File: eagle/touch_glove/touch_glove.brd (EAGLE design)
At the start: 88.9 x 50.8 mm, 210 parts, among them J2 (ID,OD)=(2.1,5.5)MM, P1 PELTIER, P2 PELTIER, P3 PELTIER, P4 PELTIER, P5 PELTIER, SW1 5A/28V, SW2 5A/28V, U1 DRV8837C, U2 DRV8837C, U3 DRV8837C, U4 DRV8837C, U5 DRV8837C, Y2 16MHz

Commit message: Started on Touch Glove.  Going full ambitious using 0402 for resistors, capacitors, and inductors
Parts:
- removed BATT1: BATTERYPTH_HOLES, MrSwirlyEyes:DUAL_PTH_PADS
- removed C121, C129: 0.1uF/50V, PiB_capacitors:_CER_SMD-805
- removed C125, C128: 10uF/25V, PiB_capacitors:_CER_SMD-805
- removed C133: 100UF/16V, PiB_capacitors:_AE_SMD_L6.6-W6.6
- removed C2, C64, C66, C68, C70, C73, C75, C80: 0.1uF/50V, MrSwirlyEyes:CAP_CER_SMD-805
- removed C23, C63, C65, C69, C71, C72, C74, C77: 10uF/25V, MrSwirlyEyes:CAP_CER_SMD-805
- removed C67, C82: 220uF/16V, MrSwirlyEyes:CAP_POL_SMD_L6.6-W6.6
- removed C78, C81: 100UF/16V, MrSwirlyEyes:CAP_POL_SMD_L6.6-W6.6
- removed C79: 1uF/25V, MrSwirlyEyes:CAP_CER_SMD-805
- removed D10: 1A/50V, PiB_discrete_semiconductors:SOD123F
- removed D6, D7, D9: 1A/50V, MrSwirlyEyes:DIODE_SMD_1A-50V-SOD123F
- removed J2: (ID,OD)=(2.1,5.5)MM, PiB_connectors:POWER_JACK_SLOT_ID2.1MM-OD5.5MM
- removed L1, L2: 10uH, MrSwirlyEyes:INDUCTOR_SMD-805
- removed P1, P2, P3, P4, P5: PELTIER, MrSwirlyEyes:CONNECTOR_PELTIER
- removed PWM_DRIVER: PCA9685, MrSwirlyEyes:TSSOP-28
- removed SW1: 5A/28V, MrSwirlyEyes:SW-SLIDE_SPDT_5A-28V_13L-7W
- removed U$1, U$2: NET_BRIDGE, MrSwirlyEyes:NET_BRIDGE
- removed U1, U2, U3, U4, U5: DRV8837C, MrSwirlyEyes:WSON-8-PPAD
- removed VIBE_1, VIBE_2, VIBE_3, VIBE_4, VIBE_5, VIBE_6: VIBE_MOTOR, MrSwirlyEyes:CONNECTOR_VIBE-MOTOR
- removed VIBE_T1, VIBE_T2, VIBE_T3, VIBE_T4, VIBE_T5, VIBE_T6: 2.6A/20V/57mΩ, MrSwirlyEyes:SOT23-3
- removed VREG2: 1.5A/3.3V, MrSwirlyEyes:SOT223-4
- removed VREG3: 1A/3.3V, MrSwirlyEyes:SOIC-8_W3.9MM
- removed VREG4: 3A/1.8V, MrSwirlyEyes:DDPAK-5
- removed VREG5: 5A/5V, PiB_ic_power:TO-263-5
- added C36, C38, C40, C45, C47, C48, C49, C50, C51: 0.1uF/50V, PiB_capacitors:_CER_SMD_0402
- added C37, C44: 10uF/16V, PiB_capacitors:_CER_SMD-603
- added C39, C43: 10uF/10V, PiB_capacitors:_CER_SMD_0402
- added C41, C42, C46: 100uF, PiB_capacitors:_CER_SMD-1210
- added D13, D14: 1A/50V, MrSwirlyEyes:DIODE_SMD_1A-50V-SOD123F
- added FLEX10, FLEX6, FLEX7, FLEX8, FLEX9: 10K, PiB:CONNECTOR_FSR
- added HBRIDGE1, HBRIDGE2, HBRIDGE3, HBRIDGE4, HBRIDGE5: DRV8837C, PiB:WSON-8-PPAD
- added Q1, Q2, Q3, Q4, Q5, Q6: MCH3474 4A/30V/50mΩ, PiB_discrete_semiconductors:SC-70FL/MCPH3
- added R38, R39, R42, R43, R44: 10KΩ, PiB_resistors:RESISTOR_SMD-0402
- added TEC1, TEC2, TEC3, TEC4, TEC5: PELTIER, PiB:CONNECTOR_PELTIER
- added VIBE1, VIBE2, VIBE3, VIBE4, VIBE5, VIBE6: VIBE_MOTOR, PiB:CONNECTOR_VIBE-MOTOR
- added VREG6: TL1963A-33 1.5A/3.3V, PiB_ic_power:SOT223-4
- added VREG7: 3A/1.8V, MrSwirlyEyes:DDPAK-5
- C1, C12, C13, C16, C17, C20, C21, C24, C25, C26, C3, C30, C31, C32, C33, C34, C4, C5, C52, C53, C54, C55, C56, C6, C7, C8, C9: device MrSwirlyEyes:CAP_CER_SMD-805 -> PiB_capacitors:_CER_SMD_0402
- C10, C11, C14, C15, C18, C19, C22, C27, C28, C29, C35, C57, C58, C59, C60, C61: value 10uF/25V -> 10uF/10V; device MrSwirlyEyes:CAP_CER_SMD-805 -> PiB_capacitors:_CER_SMD_0402
- C100, C106, C108, C116, C117, C119, C122, C124, C127, C135, C98: device PiB_capacitors:_CER_SMD-805 -> PiB_capacitors:_CER_SMD_0402
- C107, C109, C110, C111, C132, C134, C136: device PiB_capacitors:_CER_SMD-805 -> PiB_capacitors:_CER_SMD-603
- C118: value 220uF/16V -> 100uF; device PiB_capacitors:_AE_SMD_L6.6-W6.6 -> PiB_capacitors:_CER_SMD-1210
- C120, C126: value 10uF/25V -> 10uF/16V; device PiB_capacitors:_CER_SMD-805 -> PiB_capacitors:_CER_SMD-603
- C123, C97, C99: value 10uF/25V -> 10uF/10V; device PiB_capacitors:_CER_SMD-805 -> PiB_capacitors:_CER_SMD_0402
- D1, D12, D2, D3, D4, D5: value 1A/50V -> 150mA/75V; device MrSwirlyEyes:DIODE_SMD_1A-50V-SOD123F -> PiB_discrete_semiconductors:SOD-923F/0402
- FLEX1, FLEX2, FLEX3, FLEX4, FLEX5: device MrSwirlyEyes:CONNECTOR_FSR -> PiB:CONNECTOR_FSR
- L5: device PiB_leds:LED_SMD-805_ -> PiB_leds:LED_SMD-0603_
- R1, R10, R11, R12, R13, R14, R15, R16, R17, R18, R19, R2, R20, R21, R22, R23, R24, R25, R26, R27, R28, R29, R3, R30, R31, R32, R33, R34, R35, R36, R37, R4, R5, R6, R7, R8, R9: device MrSwirlyEyes:RESISTOR_SMD-805 -> PiB_resistors:RESISTOR_SMD-0402
- R46, R47: device PiB_resistors:RESISTOR_SMD-805 -> PiB_resistors:RESISTOR_SMD-0402
- moved R12 433.0 mm to (28.6, 40.3), turned to 90 degrees
- moved D12 429.7 mm to (29.2, 45.1), turned to 180 degrees
- moved C24 429.3 mm to (61.0, -15.2)
- moved R13 428.8 mm to (27.6, 40.3), turned to 90 degrees
- moved C1 425.1 mm to (29.2, 46.1)
- moved C99 415.5 mm to (39.4, 31.0), turned to 90 degrees
- moved C35 414.7 mm to (-8.38, 45.0), turned to 270 degrees
- moved ANALOG_BR 410.5 mm to (137.2, -30.5)
- moved B2 410.5 mm to (177.8, -7.62)
- moved C106 410.5 mm to (101.6, -20.3)
- moved C107 410.5 mm to (101.6, -25.4)
- moved C108 410.5 mm to (109.2, -20.3)
- moved C109 410.5 mm to (106.7, -25.4)
- moved C110 410.5 mm to (111.8, -25.4)
- moved C111 410.5 mm to (116.8, -25.4)
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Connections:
- removed net 5V: C121.1, C125.1, C133.A, D10.A, VREG5.4
- removed net BATT_-: BATT2.-, J2.GND@2
- removed net C14: DEMUX1.17
- removed net C15: DEMUX1.16
- removed net FSR_1: FLEX1.-, R11.2
- removed net FSR_2: FLEX2.-, R34.2
- removed net FSR_3: FLEX3.-, R35.2
- removed net FSR_4: FLEX4.-, R36.2
- removed net FSR_5: FLEX5.-, R37.2
- removed net N$38: L2.2, U$2.P$1
- removed net N$40: C64.1, C66.1, C67.A, C68.1, C69.1, C71.1, C72.1, C73.1, C74.1, C78.A, D6.K, D7.K, D9.K, SW1.P$1, VREG2.1, VREG3.3, VREG3.4, VREG4.1, VREG4.2
- removed net N$43: BATT1.+, SW1.P$2
- removed net PWM10: PWM_DRIVER1.17
- removed net VM: C10.1, C13.1, C14.1, C17.1, C18.1, C21.1, C22.1, C26.1, C27.1, C9.1, U1.1, U2.1, U3.1, U4.1, U5.1
- new net 1.8V: C10.1, C13.1, C14.1, C17.1, C18.1, C21.1, C22.1, C26.1, C27.1, C39.1, C40.1, C42.1, C9.1, D14.A, HBRIDGE1.1, HBRIDGE2.1, HBRIDGE3.1, HBRIDGE4.1, HBRIDGE5.1, VREG7.4, VREG7.5
- new net C8: DEMUX1.23
- new net C9: DEMUX1.22
- net 3.3V: now also C1.1, C24.1, C3.1, C35.1, C36.1, C4.1, C41.1, C43.1, C5.1, C52.1, C53.1, C54.1, C55.1, C56.1, C57.1, C58.1, C59.1, C6.1, C60.1, C61.1, C7.1, D1.K, D12.K, D13.A, D2.K, D3.K, D4.K, D5.K, VIBE1.1, VIBE2.1, VIBE3.1, VIBE4.1, VIBE5.1, VIBE6.1, VREG6.3; no longer C65.1, C75.1, C77.1, C80.1, C81.A, C82.A, D7.A, D9.A, VREG2.3, VREG4.4, VREG4.5
- net AGND: now also C30.2, C31.2, C32.2, C33.2, C34.2, C47.2, C48.2, C49.2, C50.2, C51.2, R11.1, R34.1, R35.1, R36.1, R37.1, R38.1, R39.1, R42.1, R43.1, R44.1
- net AVCC: now also C30.1, C31.1, C32.1, C33.1, C34.1, C47.1, C48.1, C49.1, C50.1, C51.1, FLEX1.+, FLEX10.+, FLEX2.+, FLEX3.+, FLEX4.+, FLEX5.+, FLEX6.+, FLEX7.+, FLEX8.+, FLEX9.+
- net BATT_+: no longer J2.PWR
- net GND: now also BATT2.-, C118.2, C36.2, C37.2, C38.2, C39.2, C40.2, C41.2, C42.2, C43.2, C44.2, C45.2, C46.2, VREG6.2, VREG6.TAB, VREG7.3, VREG7.TAB; no longer BATT1.-, C10.2, C118.K, C13.2, C14.2, C17.2, C18.2, C2.2, C21.2, C22.2, C23.2, C24.2, C26.2, C27.2, C30.2, C31.2, C32.2, C33.2, C34.2, C35.2, C52.2, C53.2, C54.2, C55.2, C56.2, C57.2, C58.2, C59.2, C60.2, C61.2, C63.2, C64.2, C65.2, C66.2, C67.K, C68.2, C69.2, C70.2, C71.2, C72.2, C73.2, C74.2, C75.2, C77.2, C78.K, C80.2, C81.K, C82.K, C9.2, J2.GND@1, L2.1, PWM_DRIVER.1, PWM_DRIVER.14, PWM_DRIVER.2, PWM_DRIVER.23, PWM_DRIVER.24, PWM_DRIVER.25, PWM_DRIVER.3, PWM_DRIVER.4, PWM_DRIVER.5, R1.1, R11.1, R12.1, R2.1, R3.1, R34.1, R35.1, R36.1, R37.1, R4.1, R5.1, U$1.P$2, U1.4, U1.GND, U2.4, U2.GND, U3.4, U3.GND, U4.4, U4.GND, U5.4, U5.GND, VIBE_T1.S, VIBE_T2.S, VIBE_T3.S, VIBE_T4.S, VIBE_T5.S, VIBE_T6.S, VREG2.2, VREG2.4, VREG3.1, VREG3.2, VREG4.3, VREG4.TAB
- net N$1: now also HBRIDGE5.3, TEC5.HOT; no longer P1.HOT, U1.2
- net N$10: now also HBRIDGE4.6, R16.2; no longer U1.6
- net N$11: now also HBRIDGE4.3, TEC4.HOT; no longer P2.HOT, U2.2
- net N$12: now also HBRIDGE3.3, TEC3.HOT; no longer P2.COLD, U2.3
- net N$13: now also HBRIDGE3.5, R18.2; no longer U2.5
- net N$14: now also HBRIDGE3.6, R20.2; no longer U2.6
- net N$15: now also Q2.3, VIBE2.2; no longer VIBE_2.2, VIBE_T2.D
- net N$16: now also HBRIDGE3.2, TEC3.COLD; no longer P3.HOT, U3.2
- net N$17: now also Q1.3, VIBE1.2; no longer VIBE_1.2, VIBE_T1.D
- net N$18: now also HBRIDGE2.3, TEC2.HOT; no longer P3.COLD, U3.3
- net N$19: now also HBRIDGE2.5, R22.2; no longer U3.5
- net N$2: now also Q4.3, VIBE4.2; no longer VIBE_4.2, VIBE_T4.D
- net N$20: now also HBRIDGE2.6, R24.2; no longer U3.6
- net N$21: now also Q4.1, R4.2; no longer VIBE_T4.G
- net N$22: now also Q5.1, R5.2; no longer VIBE_T5.G
- net N$23: now also HBRIDGE2.2, TEC2.COLD; no longer P5.HOT, U5.2
- net N$24: now also HBRIDGE1.3, TEC1.HOT; no longer P5.COLD, U5.3
- net N$25: now also HBRIDGE1.5, R26.2; no longer U5.5
- net N$26: now also HBRIDGE1.6, R28.2; no longer U5.6
- net N$27: now also HBRIDGE1.2, TEC1.COLD; no longer P4.HOT, U4.2
- net N$28: now also Q1.1, R1.2, R6.2; no longer P4.COLD, U4.3
- net N$29: now also HBRIDGE5.5, R30.2; no longer U4.5
- net N$3: now also Q5.3, VIBE5.2; no longer VIBE_5.2, VIBE_T5.D
- net N$30: now also Q6.3, VIBE6.2; no longer VIBE_6.2, VIBE_T6.D
- net N$31: now also HBRIDGE5.6, R32.2; no longer U4.6
- net N$32: now also Q6.1, R12.2; no longer VIBE_T6.G
- net N$4: now also Q3.3, VIBE3.2; no longer VIBE_3.2, VIBE_T3.D
- net N$5: now also HBRIDGE5.2, TEC5.COLD; no longer P1.COLD, U1.3
- net N$53: now also L5.2; no longer L5.K
- net N$6: now also HBRIDGE4.2, TEC4.COLD; no longer R6.2, VIBE_T1.G
- net N$7: now also Q2.1, R2.2; no longer VIBE_T2.G
- net N$8: now also HBRIDGE4.5, R14.2; no longer U1.5
- net N$9: now also Q3.1, R3.2; no longer VIBE_T3.G
- net NGND: now also C10.2, C13.2, C14.2, C17.2, C18.2, C21.2, C22.2, C24.2, C26.2, C27.2, C35.2, C52.2, C53.2, C54.2, C55.2, C56.2, C57.2, C58.2, C59.2, C60.2, C61.2, C9.2, HBRIDGE1.4, HBRIDGE1.GND, HBRIDGE1.P$1, HBRIDGE1.P$2, HBRIDGE2.4, HBRIDGE2.GND, HBRIDGE2.P$1, HBRIDGE2.P$2, HBRIDGE3.4, HBRIDGE3.GND, HBRIDGE3.P$1, HBRIDGE3.P$2, HBRIDGE4.4, HBRIDGE4.GND, HBRIDGE4.P$1, HBRIDGE4.P$2, HBRIDGE5.4, HBRIDGE5.GND, HBRIDGE5.P$1, HBRIDGE5.P$2, Q1.2, Q2.2, Q3.2, Q4.2, Q5.2, Q6.2, R1.1, R12.1, R2.1, R3.1, R4.1, R5.1; no longer C121.2, C125.2, C128.2, C129.2, C133.K, C79.2, U$1.P$1, U$2.P$2, VREG5.3, VREG5.TAB
- net SCL: no longer PWM_DRIVER.26
- net SDA: no longer PWM_DRIVER.27
- net STRAIN_1: now also FLEX3.-, R35.2
- net STRAIN_10: now also DEMUX1.16, FLEX4.-, R36.2; no longer DEMUX1.22
- net STRAIN_2: now also FLEX2.-, R34.2
- net STRAIN_3: now also FLEX1.-, R11.2
- net STRAIN_4: now also FLEX10.-, R44.2
- net STRAIN_5: now also FLEX9.-, R43.2
- net STRAIN_6: now also FLEX8.-, R42.2
- net STRAIN_7: now also FLEX7.-, R39.2
- net STRAIN_8: now also FLEX6.-, R38.2
- net STRAIN_9: now also DEMUX1.17, FLEX5.-, R37.2; no longer DEMUX1.23
- net TEC_1_COLD: now also PWM_DRIVER1.18; no longer PWM_DRIVER.7, PWM_DRIVER1.7, R26.2
- net TEC_1_HOT: now also PWM_DRIVER1.17; no longer PWM_DRIVER.6, PWM_DRIVER1.6, R28.2
- net TEC_2_COLD: now also PWM_DRIVER1.20; no longer PWM_DRIVER.9, PWM_DRIVER1.9, R22.2
- net TEC_2_HOT: now also PWM_DRIVER1.19; no longer PWM_DRIVER.8, PWM_DRIVER1.8, R24.2
- net TEC_3_COLD: now also PWM_DRIVER1.22; no longer PWM_DRIVER.11, PWM_DRIVER1.11, R18.2
- net TEC_3_HOT: now also PWM_DRIVER1.21; no longer PWM_DRIVER.10, PWM_DRIVER1.10, R20.2
- net TEC_4_COLD: no longer PWM_DRIVER.13, R14.2
- net TEC_4_HOT: no longer PWM_DRIVER.12, R16.2
- net TEC_5_COLD: no longer PWM_DRIVER.16, R30.2
- net TEC_5_HOT: no longer PWM_DRIVER.15, R32.2
- net VBATT: now also C118.1, C37.1, C38.1, C44.1, C45.1, C46.1, D13.K, D14.K, L5.1, VREG6.1, VREG7.1, VREG7.2; no longer C118.A, C128.1, C129.1, D10.K, L5.A, VREG5.1, VREG5.2
- net VCC: now also HBRIDGE1.7, HBRIDGE1.8, HBRIDGE2.7, HBRIDGE2.8, HBRIDGE3.7, HBRIDGE3.8, HBRIDGE4.7, HBRIDGE4.8, HBRIDGE5.7, HBRIDGE5.8; no longer C1.1, C2.1, C23.1, C24.1, C3.1, C30.1, C31.1, C32.1, C33.1, C34.1, C35.1, C4.1, C5.1, C52.1, C53.1, C54.1, C55.1, C56.1, C57.1, C58.1, C59.1, C6.1, C60.1, C61.1, C63.1, C7.1, C70.1, C79.1, D1.K, D12.K, D2.K, D3.K, D4.K, D5.K, D6.A, FLEX1.+, FLEX2.+, FLEX3.+, FLEX4.+, FLEX5.+, L1.1, L1.2, PWM_DRIVER.28, U1.7, U1.8, U2.7, U2.8, U3.7, U3.8, U4.7, U4.8, U5.7, U5.8, VIBE_1.1, VIBE_2.1, VIBE_3.1, VIBE_4.1, VIBE_5.1, VIBE_6.1, VREG3.5, VREG3.6
- net VIBE_1: now also PWM_DRIVER1.6; no longer PWM_DRIVER.17, PWM_DRIVER1.18, R1.2
- net VIBE_2: now also PWM_DRIVER1.7; no longer PWM_DRIVER.18, PWM_DRIVER1.19, R2.2
- net VIBE_3: now also PWM_DRIVER1.8; no longer PWM_DRIVER.19, PWM_DRIVER1.20, R3.2
- net VIBE_4: now also PWM_DRIVER1.9; no longer PWM_DRIVER.20, PWM_DRIVER1.21, R4.2
- net VIBE_5: now also PWM_DRIVER1.10; no longer PWM_DRIVER.21, PWM_DRIVER1.22, R5.2
- net VIBE_6: now also PWM_DRIVER1.11; no longer PWM_DRIVER.22, R12.2
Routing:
- net AVCC: track 0.00 -> 138.7 mm
- net STRAIN_3: track 0.00 -> 65.3 mm
- net STRAIN_2: track 0.00 -> 59.6 mm
- net 3.3V: track 0.00 -> 56.7 mm
- net 1.8V: track 0.00 -> 56.5 mm
- net STRAIN_1: track 0.00 -> 54.0 mm
- net STRAIN_10: track 0.00 -> 37.9 mm
- net STRAIN_9: track 0.00 -> 33.5 mm
- net STRAIN_4: track 0.00 -> 30.7 mm
- net STRAIN_5: track 0.00 -> 27.0 mm
- net STRAIN_6: track 0.00 -> 23.2 mm
- net AGND: track 0.00 -> 22.2 mm, vias 0 -> 24
- net VIBE_1: track 0.00 -> 21.9 mm
- net STRAIN_7: track 0.00 -> 19.5 mm
- net NGND: track 0.00 -> 18.1 mm, vias 0 -> 14
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- added copper zone on layer 16, net NGND
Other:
- board size 88.9 x 50.8 mm -> 84 x 50.8 mm

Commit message: Touch Glove Rev 1: Restarted board.  Layout for DEMUX + FLEX sensors completed
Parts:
- removed C11, C15, C19, C28, C29: 10uF/10V, PiB_capacitors:_CER_SMD_0402
- R11, R34, R35, R36, R37, R38, R39, R42, R43, R44: value 10KΩ -> 47KΩ
- moved L7 274.5 mm to (-74.9, 52.1)
- moved R47 269.2 mm to (-59.7, 80.0)
- moved L6 264.6 mm to (-69.8, 52.1)
- moved R46 262.2 mm to (-57.1, 80.0)
- moved C122 244.1 mm to (-80.0, 68.6)
- moved R48 234.7 mm to (-26.7, 57.1)
- moved B2 233.5 mm to (-49.5, 45.7)
- moved NOISE_BR 231.8 mm to (-64.8, 78.7)
- moved L3 230.6 mm to (-80.0, 52.1)
- moved C135 228.0 mm to (-22.9, 72.4)
- moved ANALOG_BR 227.3 mm to (-62.2, 78.7)
- moved C119 226.5 mm to (-76.2, 68.6)
- moved L5 218.1 mm to (-24.1, 61.0)
- moved C117 216.0 mm to (-72.4, 68.6)
- moved D11 215.3 mm to (-61.0, 47.0)
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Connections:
- net GND: no longer C11.2, C15.2, C19.2, C28.2, C29.2
- net STRAIN_1: now also FLEX2.-, R34.2; no longer FLEX3.-, R35.2
- net STRAIN_10: now also FLEX6.-, R38.2; no longer FLEX4.-, R36.2
- net STRAIN_2: now also FLEX7.-, R39.2; no longer FLEX2.-, R34.2
- net STRAIN_3: now also FLEX3.-, R35.2; no longer FLEX1.-, R11.2
- net STRAIN_4: now also FLEX8.-, R42.2; no longer FLEX10.-, R44.2
- net STRAIN_5: now also FLEX4.-, R36.2; no longer FLEX9.-, R43.2
- net STRAIN_6: now also FLEX9.-, R43.2; no longer FLEX8.-, R42.2
- net STRAIN_7: now also FLEX5.-, R37.2; no longer FLEX7.-, R39.2
- net STRAIN_8: now also FLEX10.-, R44.2; no longer FLEX6.-, R38.2
- net STRAIN_9: now also FLEX1.-, R11.2; no longer FLEX5.-, R37.2
- net VCC: no longer C11.1, C15.1, C19.1, C28.1, C29.1
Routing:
- net 3.3V: track 56.7 -> 0.00 mm
- net 1.8V: track 56.5 -> 0.00 mm
- net AVCC: track 138.7 -> 88.2 mm
- net STRAIN_3: track 65.3 -> 15.4 mm
- net STRAIN_2: track 59.6 -> 14.1 mm
- net STRAIN_1: track 54.0 -> 19.4 mm
- net STRAIN_10: track 37.9 -> 15.1 mm
- net VIBE_1: track 21.9 -> 0.00 mm
- net STRAIN_4: track 30.7 -> 10.2 mm
- net NGND: track 18.1 -> 0.00 mm, vias 14 -> 0
- net VIBE_2: track 17.5 -> 0.00 mm
- net STRAIN_9: track 33.5 -> 18.7 mm
- net VIBE_3: track 13.3 -> 0.00 mm
- net STRAIN_6: track 23.2 -> 11.8 mm
- net STRAIN_5: track 27.0 -> 17.0 mm
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- added copper zone on layer 16, net AGND
- removed copper zone on layer 16, net NGND
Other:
- board size 84 x 50.8 mm -> 76.2 x 50.8 mm

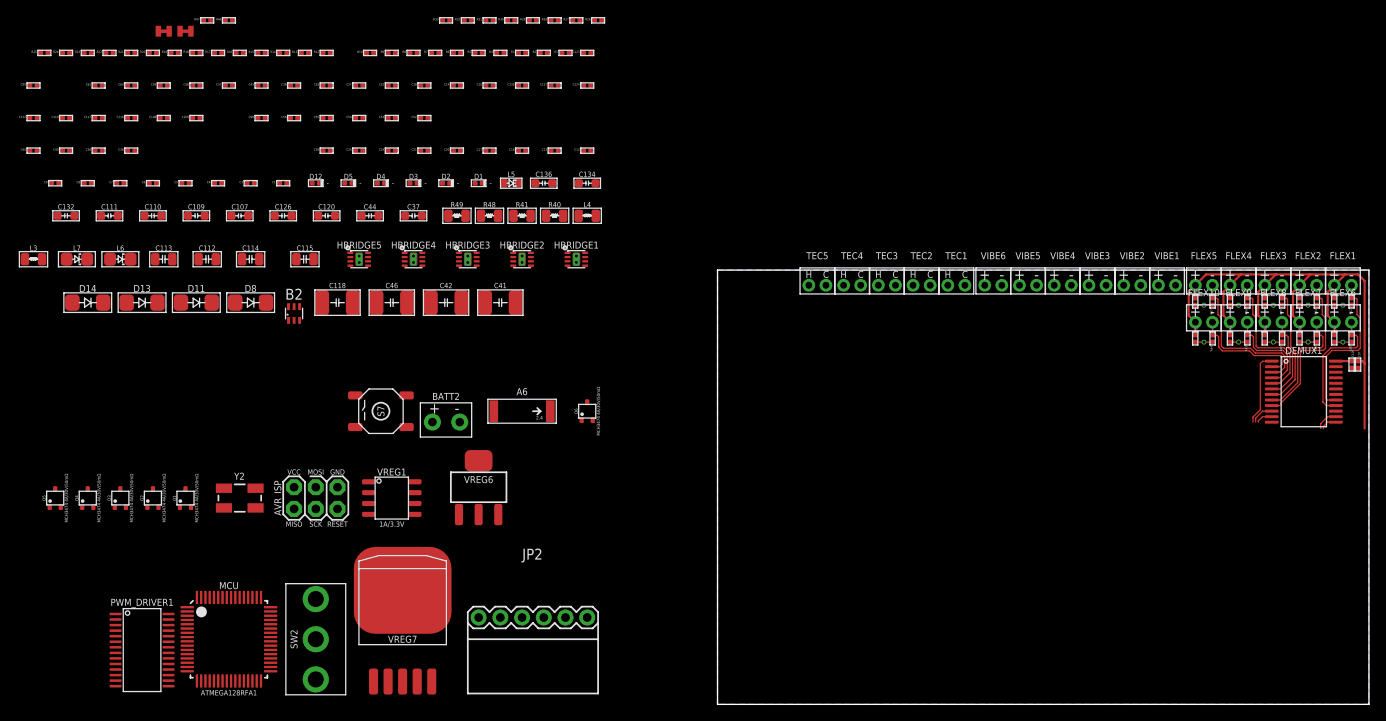
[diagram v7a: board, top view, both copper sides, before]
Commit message: Touch Glove Rev 1: Routed Vibe motor, TEC + H Bridge, and PWM Driver
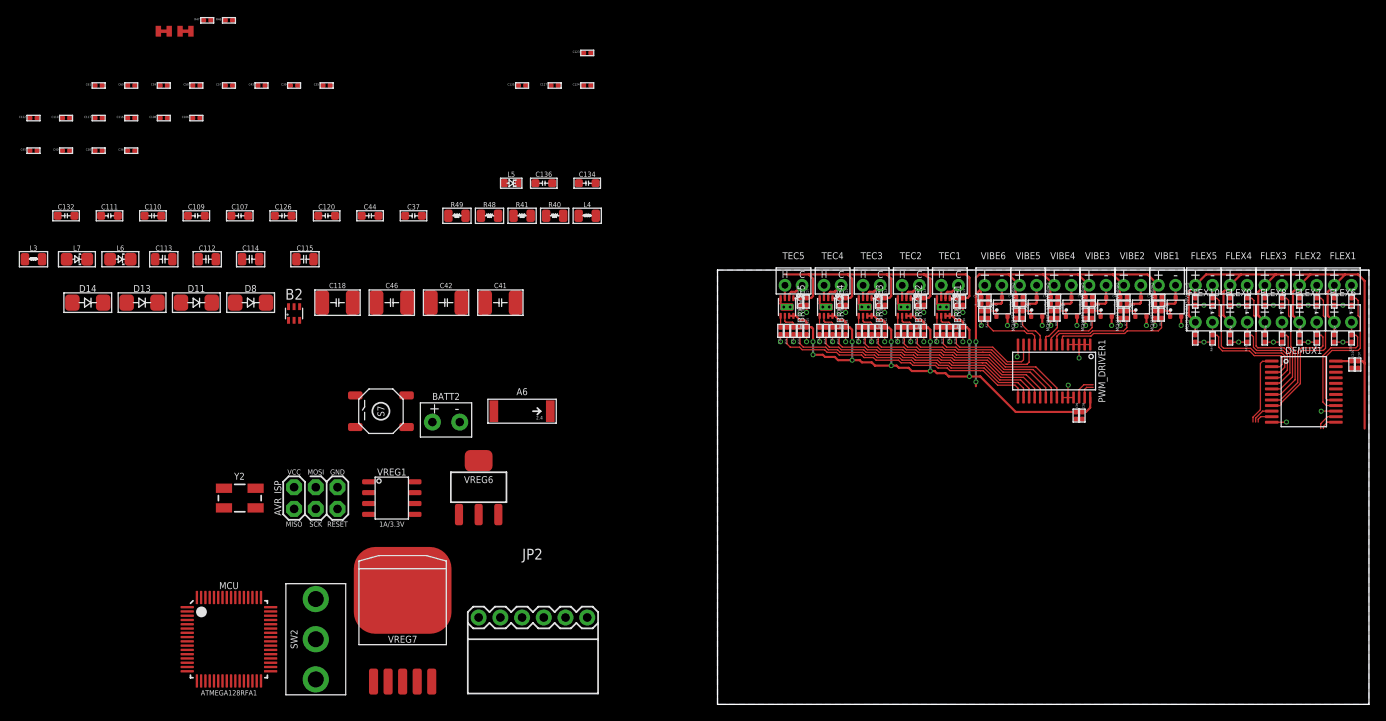
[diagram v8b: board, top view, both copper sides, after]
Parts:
- removed C24, C52, C53, C54, C55, C56: 0.1uF/50V, PiB_capacitors:_CER_SMD_0402
- moved C99 127.9 mm to (41.9, 33.8), turned to 270 degrees
- moved Q1 118.0 mm to (53.6, 46.5)
- moved Q2 117.7 mm to (49.5, 46.5)
- moved Q3 117.5 mm to (45.5, 46.5)
- moved Q4 117.2 mm to (41.4, 46.5)
- moved Q5 117.0 mm to (37.3, 46.5)
- moved PWM_DRIVER1 111.6 mm to (39.4, 39.0), turned to 270 degrees
- moved R25 107.2 mm to (23.4, 43.7), turned to 90 degrees
- moved C3 107.0 mm to (51.6, 47.6)
- moved C4 106.8 mm to (47.5, 47.6)
- moved C5 106.5 mm to (43.4, 47.6)
- moved C6 106.3 mm to (39.4, 47.6)
- moved C7 106.0 mm to (35.3, 47.6)
- moved R24 104.0 mm to (22.6, 43.7), turned to 90 degrees
- moved C98 102.1 mm to (42.7, 33.8), turned to 270 degrees
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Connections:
- net 3.3V: no longer C24.1, C52.1, C53.1, C54.1, C55.1, C56.1
- net NGND: no longer C24.2, C52.2, C53.2, C54.2, C55.2, C56.2
- net TEC_1_COLD: now also PWM_DRIVER1.12; no longer PWM_DRIVER1.18
- net TEC_1_HOT: now also PWM_DRIVER1.13; no longer PWM_DRIVER1.17
- net TEC_2_COLD: now also PWM_DRIVER1.21; no longer PWM_DRIVER1.20
- net TEC_2_HOT: now also PWM_DRIVER1.22; no longer PWM_DRIVER1.19
- net TEC_3_COLD: now also PWM_DRIVER1.19; no longer PWM_DRIVER1.22
- net TEC_3_HOT: now also PWM_DRIVER1.20; no longer PWM_DRIVER1.21
- net TEC_4_COLD: now also PWM_DRIVER1.17; no longer PWM_DRIVER1.13
- net TEC_4_HOT: now also PWM_DRIVER1.18; no longer PWM_DRIVER1.12
- net TEC_5_COLD: now also PWM_DRIVER1.15; no longer PWM_DRIVER1.16
- net TEC_5_HOT: now also PWM_DRIVER1.16; no longer PWM_DRIVER1.15
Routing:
- net VCC: track 0.00 -> 76.7 mm, vias 0 -> 10
- net 3.3V: track 0.00 -> 57.4 mm, vias 0 -> 2
- net 1.8V: track 0.00 -> 47.1 mm
- net TEC_5_COLD: track 0.00 -> 31.4 mm
- net TEC_5_HOT: track 0.00 -> 30.5 mm
- net TEC_4_COLD: track 0.00 -> 28.1 mm
- net TEC_4_HOT: track 0.00 -> 27.2 mm
- net NGND: track 0.00 -> 26.1 mm, vias 0 -> 22
- net TEC_3_COLD: track 0.00 -> 24.8 mm
- net TEC_3_HOT: track 0.00 -> 24.0 mm
- net TEC_2_COLD: track 0.00 -> 21.6 mm
- net GND: track 0.00 -> 21.1 mm, vias 0 -> 18
- net TEC_2_HOT: track 0.00 -> 20.8 mm
- net TEC_1_COLD: track 0.00 -> 14.3 mm
- net VIBE_1: track 0.00 -> 14.1 mm
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- added copper zone on layer 16, net NGND
- removed copper zone on layer 16, net AGND
